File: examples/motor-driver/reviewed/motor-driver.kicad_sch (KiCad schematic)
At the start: 12 parts, among them J1 VM 2.7-10.8V, J2 MOTOR A, J3 MOTOR B, J4 LOGIC, U1 DRV8833PW

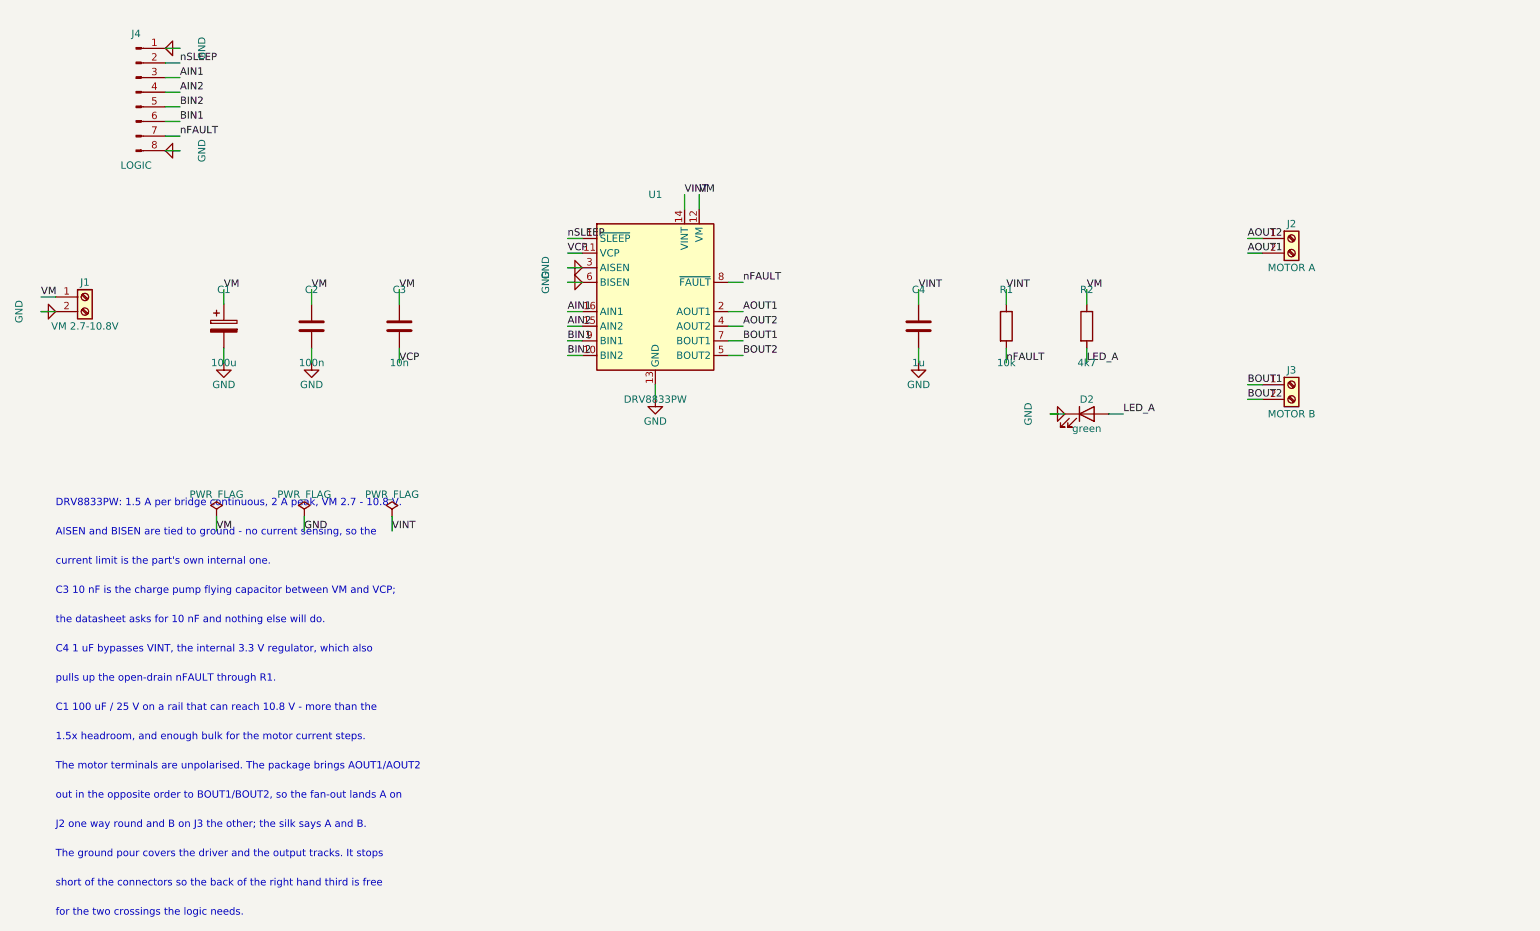
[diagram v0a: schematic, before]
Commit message: Route the sheets, and anchor the ground vias where the loop is
The user's verdict on the last round stood: none of the five schematics
read as a human drawing, and the artwork still had its physics wrong.
This round answers both.

The schematic side replaces the stub-and-label sheet with a router.
Every signal net becomes a tree of straight, L-, Z- and detour-shaped
runs on the 1.27 mm grid: legs leave a pin along its own stub, escape
distances stagger so a bus does not fight over one column, every pin
reserves a runway another wire may cross but not ride along, and the
sheet frame, title block and notes are obstacles like any symbol.
Fragments merge Kruskal-style so a rail whose regulator is boxed in
still gets its capacitors chained; each surviving fragment keeps one
label, because the label is what names the net. Collinear same-net
segments are unioned and then split at every tee - KiCad 9's
connectivity requires files drawn the way the editor draws them, with
a junction dot and a wire break wherever a branch tees in, and a wire
that runs through a junction connects on one side of it only. That
last fact cost an evening and is now a comment.

Trying to draw the wires found what no rule had: the buck's LED was
upside down with its ground pointing up into the resistor above it,
both breakout headers faced away from everything they connect to
(fixed with mirrored symbols, which Part now supports), the FPGA
sheet's notes printed over the 1.2 V regulator, and its programming
header sat inside the title block. Wired: buck, motor and op-amp
completely; the Pico carrier 31 of 33 nets; the FPGA board 16 of 19 -
what stays labelled is what a human would label too.

The artwork side anchors every FPGA decoupling capacitor's ground via
against its own pad, on the far side from the supply pad, with the
1.2 mm stub as the whole loop - retiring all seven
layout.decoupling_via findings and that waiver with them. A back_cost
experiment (0.4 to 0.6) to shrink the return-path cuts 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
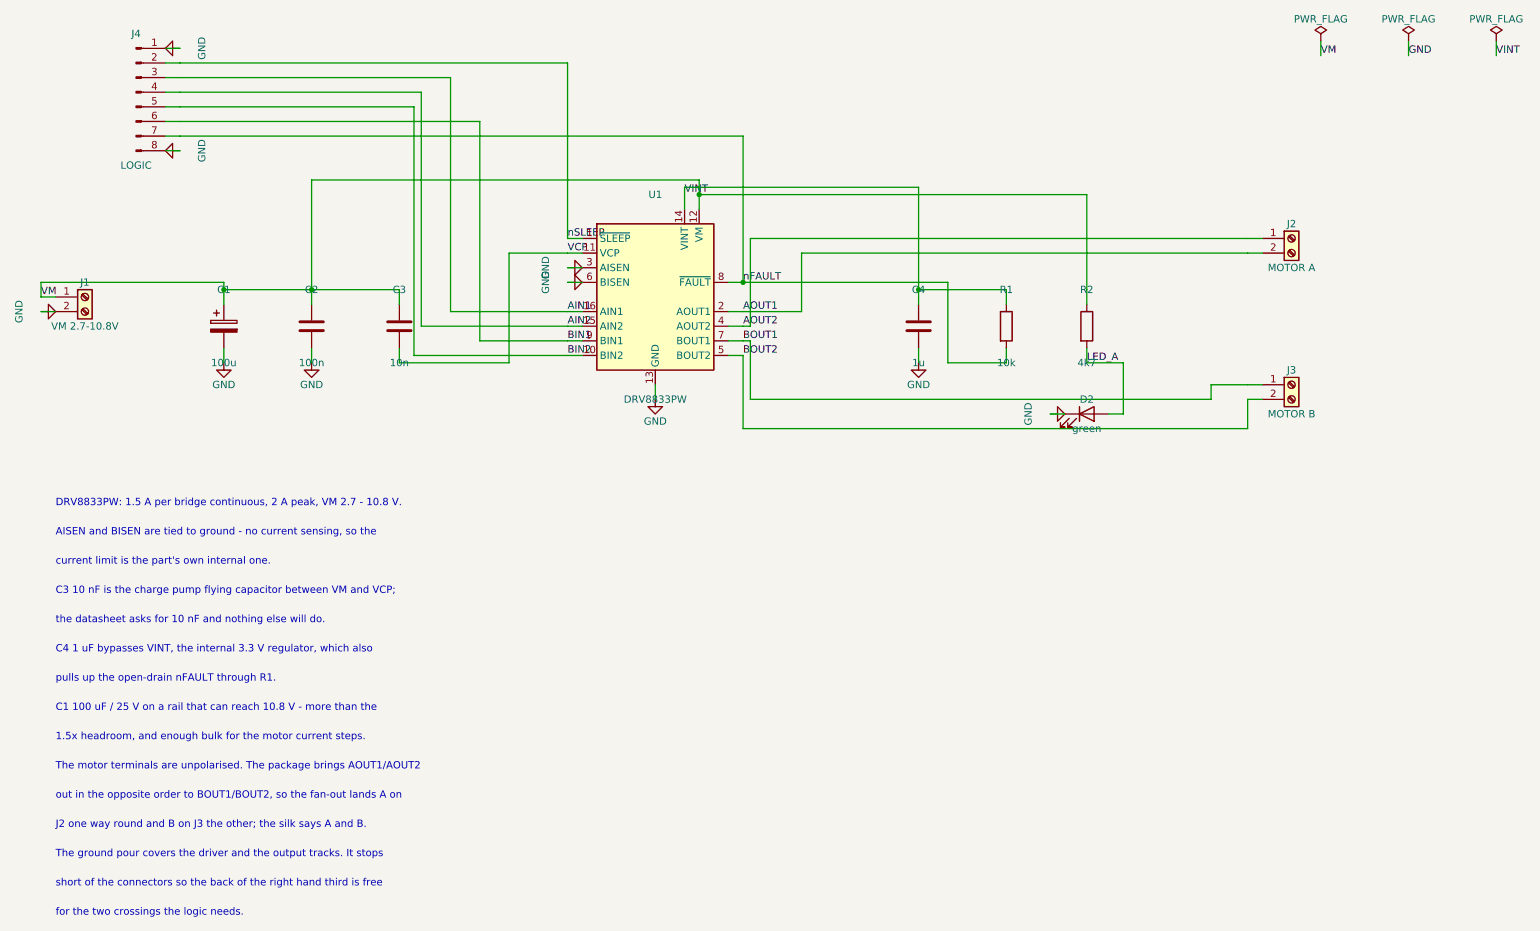
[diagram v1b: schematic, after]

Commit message: Regenerate the five with stitched pours, silk that speaks, and wires that never double back
All ten variants rebuilt by the fixed generator: reviewed boards carry
ground on both faces with the stitching ring (buck 35 vias, fpga 116),
thru_hole_only front pours, the board id and connector pin names in
silk, and the buck's explicit ground return; the sheets hook power up
through upright symbols and source-anchored flags with no overlapping
wires and no junction-less tees left. Every reviewed variant passes its
own gate with zero errors; every as-generated variant still fails, now
also for the rules this round added.

Co-Authored-By: Claude Fable 5 <noreply@anthropic.com>
Claude-Session: https://claude.ai/code/session_01DUj7Ltu92tWg159mCSacwY
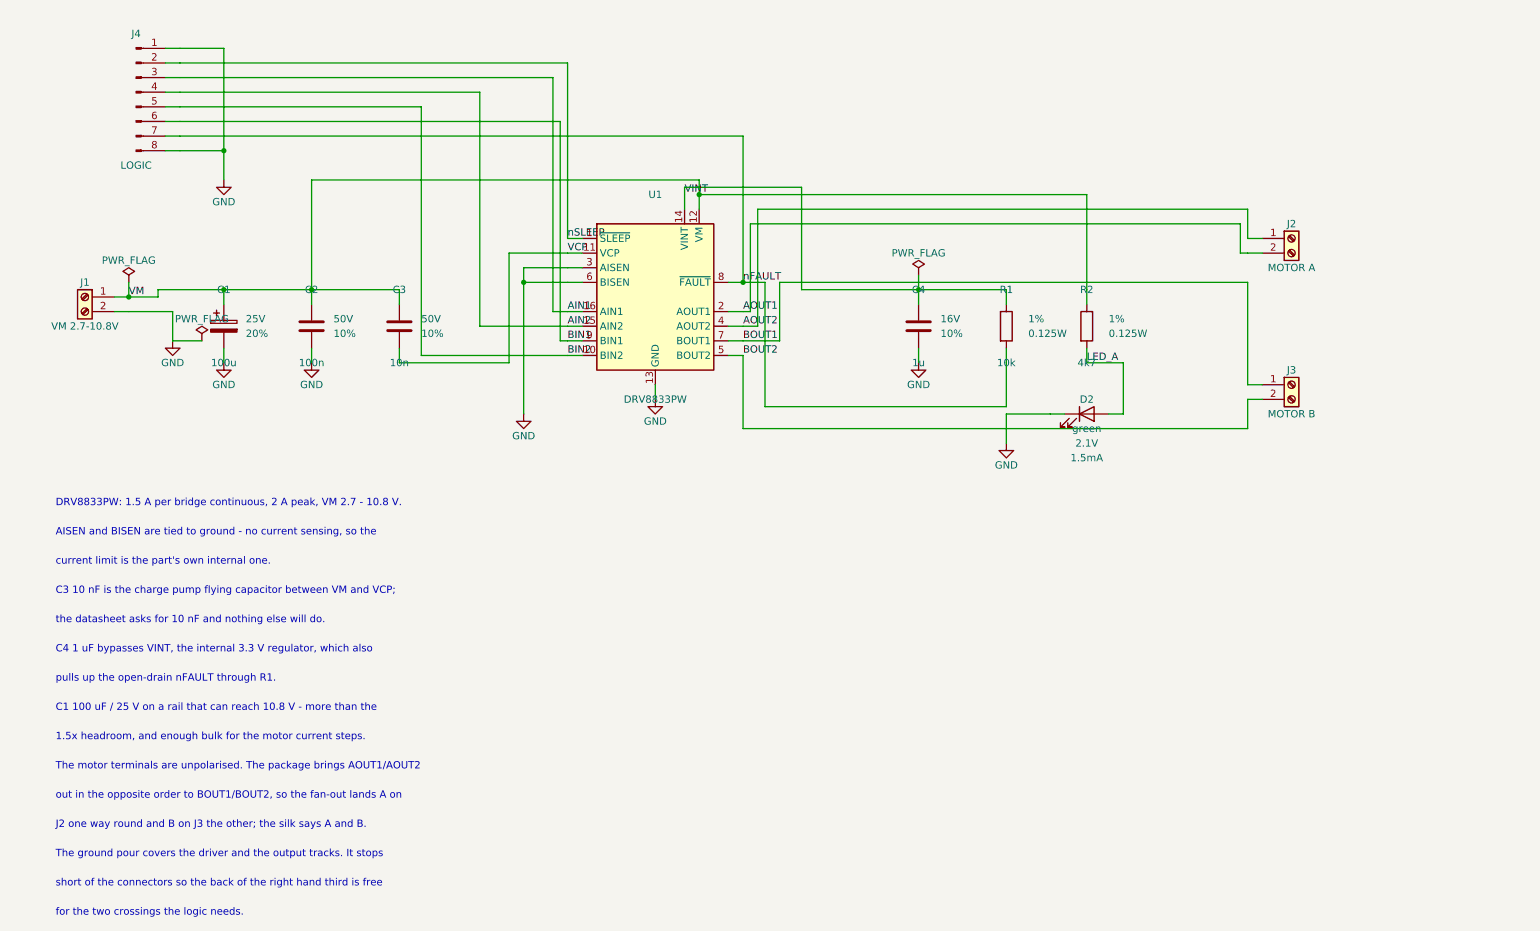
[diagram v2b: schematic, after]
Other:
- moved on the sheet: J1
